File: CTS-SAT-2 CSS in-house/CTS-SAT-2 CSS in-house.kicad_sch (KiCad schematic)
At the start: 56 parts, among them J1 3v3, J2 GND, J3 SCL I2c, J4 SDA I2c, U1 POPA4383PWR, U2 POPA4383PWR, U3 ADS7128IRTET

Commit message: initial + footprints
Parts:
- LED1, LED2, LED3, LED4, LED5, LED6, LED7, LED8: footprint 6p550-5363p01-4_VIS -> 6p550-5363p01-4_VIS footprints:6p550-5363p01-4_VIS
- U1, U2: footprint TSSOP_PW_14_TEX -> ul_POPA4383PWR footprints:TSSOP_PW_14_TEX
- U3: footprint WQFN16_RTE_TEX -> WQFN16_RTE_TEX-M footprints:WQFN16_RTE_TEX
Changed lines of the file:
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@@
 			)
 		)
-		(property "Footprint" "6p550-5363p01-4_VIS"
+		(property "Footprint" "6p550-5363p01-4_VIS footprints:6p550-5363p01-4_VIS"
 			(at 180.34 25.4 0)
 			(hide yes)
@@
 			)
 		)
-		(property "Footprint" "6p550-5363p01-4_VIS"
+		(property "Footprint" "6p550-5363p01-4_VIS footprints:6p550-5363p01-4_VIS"
 			(at 58.42 78.74 0)
 			(hide yes)
@@
 			)
 		)
-		(property "Footprint" "WQFN16_RTE_TEX"
+		(property "Footprint" "WQFN16_RTE_TEX-M footprints:WQFN16_RTE_TEX"
 			(at 201.93 71.12 0)
 			(hide yes)
@@
 			)
 		)
-		(property "Footprint" "6p550-5363p01-4_VIS"
+		(property "Footprint" "6p550-5363p01-4_VIS footprints:6p550-5363p01-4_VIS"
 			(at 58.42 50.8 0)
 			(hide yes)
@@
 			)
 		)
-		(property "Footprint" "6p550-5363p01-4_VIS"
+		(property "Footprint" "6p550-5363p01-4_VIS footprints:6p550-5363p01-4_VIS"
 			(at 58.42 104.14 0)
 			(hide yes)
@@
 			)
 		)
-		(property "Footprint" "6p550-5363p01-4_VIS"
+		(property "Footprint" "6p550-5363p01-4_VIS footprints:6p550-5363p01-4_VIS"
 			(at 58.42 64.77 0)
 			(hide yes)
@@
 			)
 		)
-		(property "Footprint" "TSSOP_PW_14_TEX"
+		(property "Footprint" "ul_POPA4383PWR footprints:TSSOP_PW_14_TEX"
 			(at 97.79 27.94 0)
 			(hide yes)
@@
 			)
 		)
-		(property "Footprint" "6p550-5363p01-4_VIS"
+		(property "Footprint" "6p550-5363p01-4_VIS footprints:6p550-5363p01-4_VIS"
 			(at 58.42 36.83 0)
 			(hide yes)
@@
 			)
 		)
-		(property "Footprint" "6p550-5363p01-4_VIS"
+		(property "Footprint" "6p550-5363p01-4_VIS footprints:6p550-5363p01-4_VIS"
 			(at 58.42 20.32 0)
 			(hide yes)
@@
 			)
 		)
-		(property "Footprint" "6p550-5363p01-4_VIS"
+		(property "Footprint" "6p550-5363p01-4_VIS footprints:6p550-5363p01-4_VIS"
 			(at 58.42 91.44 0)
 			(hide yes)
@@
 			)
 		)
-		(property "Footprint" "TSSOP_PW_14_TEX"
+		(property "Footprint" "ul_POPA4383PWR footprints:TSSOP_PW_14_TEX"
 			(at 99.06 85.09 0)
 			(hide yes)

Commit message: Reorganized Schematic
Reorganized the structure of the schematic, using boxes and labels. Eliminated anything that was overlapping and improved readability.
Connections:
- net at C14.2, C4.2, R15.2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: no longer U3.16 (AIN1/GPIO1)
- net ARRAY_SIGNAL_4: now reaches C15.1, C6.1, LED5.1 (ANODE), R16.1, U2.2 (-IN_A)
- net TIA_OUTPUT_4: now reaches C15.2, C6.2, R6.2, U2.1 (OUT_A), U3.3 (AIN4/GPIO4)
- net ARRAY_SIGNAL_6: now reaches C11.1, C17.1, R8.1, U2.13 (-IN_D)
- net ARRAY_SIGNAL_6: now also LED8.1 (ANODE); no longer LED7.1 (ANODE)
- net TIA_OUTPUT_6: now reaches C11.2, C17.2, R18.2, U2.14 (OUT_D)
- net TIA_OUTPUT_6: now also U3.5 (AIN6/GPIO6); no longer U3.4 (AIN5/GPIO5)
- net ARRAY_SIGNAL_7: now reaches C12.1, C18.1, R9.1, U2.9 (-IN_C)
- net ARRAY_SIGNAL_7: now also LED7.1 (ANODE); no longer LED8.1 (ANODE)
- net TIA_OUTPUT_7: now reaches C12.2, C18.2, R19.2, U2.8 (OUT_C)
- net TIA_OUTPUT_7: now also U3.6 (AIN7/GPIO7); no longer U3.5 (AIN6/GPIO6)
- net at C19.1, C20.1, J1.1 (Pin_1)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: no longer C21.2, C22.2
- net ARRAY_SIGNAL_5: now reaches C10.1, C16.1, LED6.1 (ANODE), R17.1, U2.6 (-IN_B)
- net TIA_OUTPUT_3: now reaches C13.2, C5.2, R14.2, U1.8 (OUT_C)
- net TIA_OUTPUT_3: now also U3.2 (AIN3/GPIO3); no longer U3.1 (AIN2/GPIO2)
- net TIA_OUPTUT_1: now reaches C2.2, C7.2, R12.2, U1.1 (OUT_A)
- net TIA_OUPTUT_1: now also U3.16 (AIN1/GPIO1); no longer U3.15 (AIN0/GPIO0)
- net TIA_OUTPUT_2: now reaches C3.2, C8.2, R13.2, U1.7 (OUT_B)
- net TIA_OUTPUT_2: now also U3.1 (AIN2/GPIO2); no longer U3.2 (AIN3/GPIO3)
- net TIA_OUTPUT_5: now reaches C10.2, C16.2, R7.2, U2.7 (OUT_B)
- net TIA_OUTPUT_5: now also U3.4 (AIN5/GPIO5); no longer U3.6 (AIN7/GPIO7)
- net ARRAY_SIGNAL_3: now reaches C13.1, C5.1, LED4.1 (ANODE), R5.1, U1.9 (-IN_C)
- net ARRAY_SIGNAL_2: now reaches C3.1, C8.1, LED3.1 (ANODE), R3.1, U1.6 (-IN_B)
- net ARRAY_SIGNAL_1: now reaches C2.1, C7.1, LED2.1 (ANODE), R2.1, U1.2 (-IN_A)
- net at R17.2: no longer R7.1
- net Earth renamed GND
- net GND: no longer U3.17 (GND)
- new net COARSE_TIA_OUTPUT: U3.15 (AIN0/GPIO0)
- now unconnected: J4.1 (Pin_1), R21.2, U3.14 (SDA)
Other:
- note added: "ADC"
- note added: "Photodiode Array"
- note added: "TIA 1 CIRCUIT"
- note added: "TIA 2 CIRCUIT"
- moved on the sheet: C10, C11, C12, C13, C14, C15, C16, C17, C18, C19, C2, C20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

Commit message: Fixing from comments
Changed some basic things from comments, organization, correcting footprints.
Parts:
- removed J1: 3v3, Connector_PinHeader_2.54mm:PinHeader_1x01_P2.54mm_Vertical, symbol Connector_Generic:Conn_01x01
- removed J2: GND, Connector_PinHeader_2.54mm:PinHeader_1x01_P2.54mm_Vertical, symbol Connector_Generic:Conn_01x01
- removed J3: SCL I2c, Connector_PinHeader_2.54mm:PinHeader_1x01_P2.54mm_Vertical, symbol Connector_Generic:Conn_01x01
- removed J4: SDA I2c, Connector_PinHeader_2.54mm:PinHeader_1x01_P2.54mm_Vertical, symbol Connector_Generic:Conn_01x01
- added J1: Conn_01x04_Socket, Connector:FanPinHeader_1x04_P2.54mm_Vertical, symbol Connector:Conn_01x04_Socket
- R10, R11: now not fitted
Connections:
- net GND: now also U3.17 (GND), J1.3 (Pin_3)
- net 3V3_POWER: now reaches C19.1, C20.1, R21.1, R22.1, U3.10 (DVDD), U3.7 (AVDD)
- net 3V3_POWER: now also J1.4 (Pin_4)
- net at R21.2: now also U3.14 (SDA), J1.1 (Pin_1)
- net at R22.2, U3.13 (SCL): now also J1.2 (Pin_2)
- net 3V3_SUPPLY_1: now reaches C22.2
- net 3V3_SUPPLY_2: now reaches C21.2

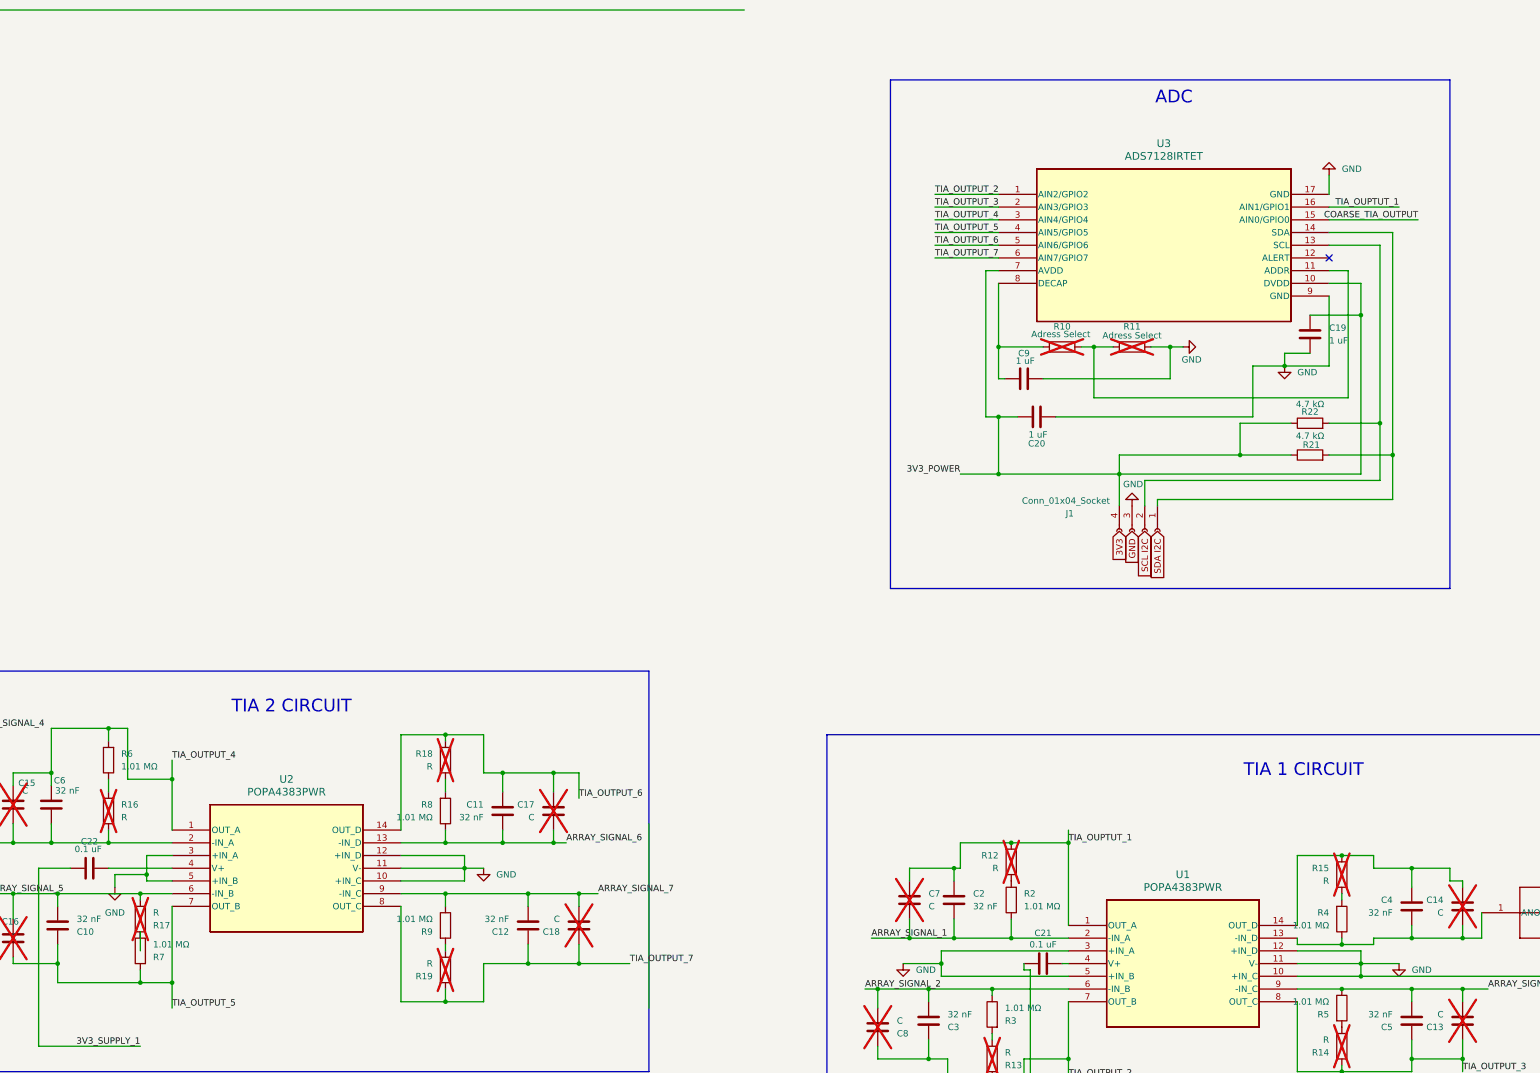
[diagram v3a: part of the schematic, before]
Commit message: More changes
Added voltage divider for virtual ground
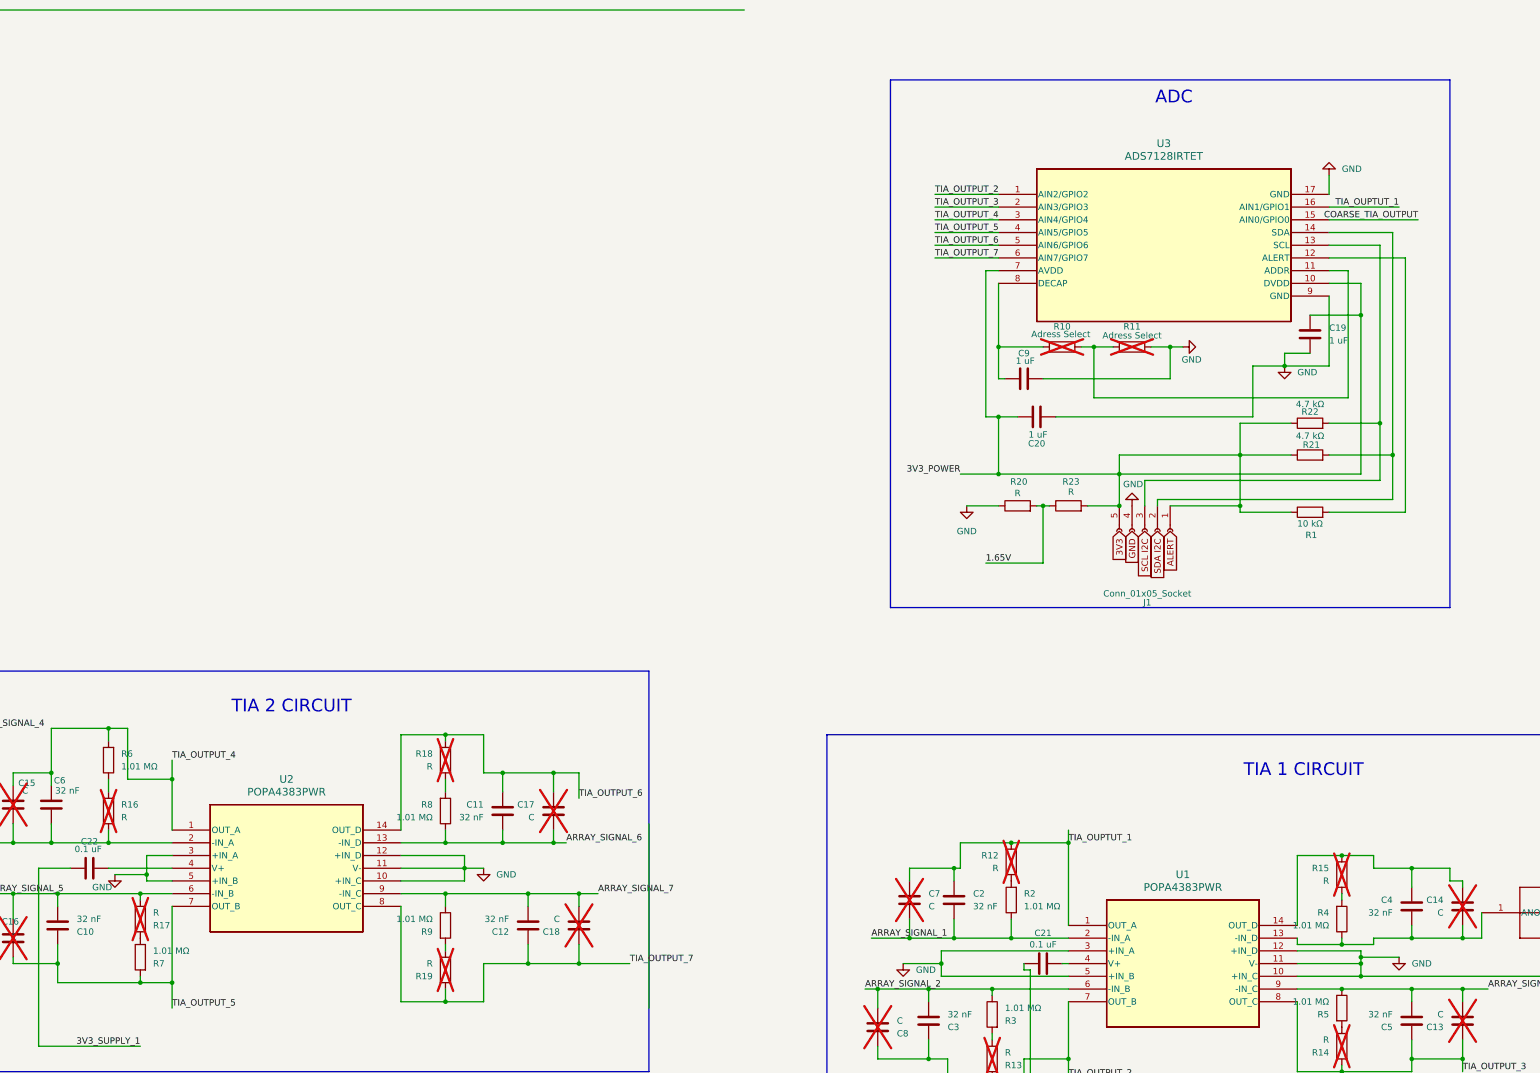
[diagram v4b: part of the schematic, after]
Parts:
- removed J1: Conn_01x04_Socket, Connector:FanPinHeader_1x04_P2.54mm_Vertical, symbol Connector:Conn_01x04_Socket
- added J1: Conn_01x05_Socket, symbol Connector:Conn_01x05_Socket
- added R1: 10 kΩ, Resistor_SMD:R_0201_0603Metric_Pad0.64x0.40mm_HandSolder, symbol Device:R
- added R20, R23: R, symbol Device:R
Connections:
- net 3V3_POWER: now also J1.1 (Pin_1), J1.5 (Pin_5), R1.1, R23.2
- net GND: now also J1.4 (Pin_4), R20.1
- net at R21.2, U3.14 (SDA): now also J1.2 (Pin_2)
- net at R22.2, U3.13 (SCL): now also J1.3 (Pin_3)
- net at U3.12 (ALERT): now also R1.2
- net at R17.2: now also R7.1
- new net 1.65V: R20.2, R23.1
- no-connect marks 1 -> 0
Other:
- moved on the sheet: R7

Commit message: Finished all comments
Completed all comments from the design review, changed DNP to sockets for testing, added virtual ground for TIAs, and other small things
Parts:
- removed C13, C14, C15, C16, C17, C18, C7, C8: C, Capacitor_SMD:C_1206_3216Metric_Pad1.33x1.80mm_HandSolder, symbol Device:C
- removed R12, R13, R14, R15, R16, R17, R18, R19: R, Resistor_SMD:R_1206_3216Metric_Pad1.30x1.75mm_HandSolder, symbol Device:R
- removed R21: 4.7 kΩ, Resistor_SMD:R_0603_1608Metric_Pad0.98x0.95mm_HandSolder, symbol Device:R
- added J10, J11, J12, J13, J14, J15, J16, J17, J2, J3, J4, J5, J6, J7, J8, J9: Socket_1x2, Connector_PinSocket_2.54mm:PinSocket_1x02_P2.54mm_Vertical, symbol Connector:Conn_01x02_Socket
- added R24: 4.7 kΩ, Resistor_SMD:R_0603_1608Metric_Pad0.98x0.95mm_HandSolder, symbol Device:R
- J1: footprint (none) -> Connector_PinHeader_2.54mm:PinHeader_1x05_P2.54mm_Vertical
- R20, R23: value R -> 10 kΩ; footprint (none) -> Resistor_SMD:R_0201_0603Metric_Pad0.64x0.40mm_HandSolder
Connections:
- net 3V3_SUPPLY_2 is gone; now on net 3V3_SUPPLY_1: C21.2
- net 3V3_SUPPLY_1: now also C19.1, C20.1, J1.5 (Pin_5), R1.1, R22.1, R23.2, U3.10 (DVDD), U3.7 (AVDD), R24.1
- net ARRAY_SIGNAL_1: now also J8.2 (Pin_2)
- net ARRAY_SIGNAL_2: now also J11.1 (Pin_1)
- net ARRAY_SIGNAL_3: now also J15.1 (Pin_1)
- net ARRAY_SIGNAL_4: now also J2.2 (Pin_2), J3.2 (Pin_2)
- net ARRAY_SIGNAL_5: now also J16.1 (Pin_1), J17.1 (Pin_1)
- net ARRAY_SIGNAL_6: now also J5.2 (Pin_2)
- net ARRAY_SIGNAL_7: now also J7.1 (Pin_1)
- net GND: no longer U1.10 (+IN_C), U1.12 (+IN_D), U1.3 (+IN_A), U1.5 (+IN_B), U2.10 (+IN_C), U2.12 (+IN_D), U2.3 (+IN_A), U2.5 (+IN_B)
- net TIA_OUPTUT_1: now also J8.1 (Pin_1), J9.1 (Pin_1)
- net TIA_OUTPUT_2: now also J10.2 (Pin_2), J11.2 (Pin_2)
- net TIA_OUTPUT_3: now also J14.2 (Pin_2), J15.2 (Pin_2)
- net TIA_OUTPUT_4: now also J2.1 (Pin_1)
- net TIA_OUTPUT_5: now also J16.2 (Pin_2)
- net TIA_OUTPUT_6: now also J4.1 (Pin_1), J5.1 (Pin_1)
- net TIA_OUTPUT_7: now also J6.2 (Pin_2), J7.2 (Pin_2)
- net at C4.1, LED1.1 (ANODE), R4.1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: now also J13.2 (Pin_2)
- net COURSE_TIA_OUTPUT: now reaches C4.2, U1.14 (OUT_D)
- net COURSE_TIA_OUTPUT: now also J12.1 (Pin_1), J13.1 (Pin_1)
- net at J1.2 (Pin_2): now also R22.2, U3.13 (SCL); no longer U3.14 (SDA)
- net at R1.2, U3.12 (ALERT): now also J1.3 (Pin_3)
- net at R3.2: now also J10.1 (Pin_1)
- net at R8.2: now also J4.2 (Pin_2)
- net at R4.2: now also J12.2 (Pin_2)
- net at R5.2: now also J14.1 (Pin_1)
- net at R9.2: now also J6.1 (Pin_1)
- net at R2.2: now also J9.2 (Pin_2)
- net at R7.1: now also J17.2 (Pin_2)
- net at R6.1: now also J3.1 (Pin_1)
- net 1.65V renamed 1.65V_VGND_1
- net 1.65V_VGND_1: now also U1.10 (+IN_C), U1.12 (+IN_D), U1.3 (+IN_A), U1.5 (+IN_B), U2.3 (+IN_A), U2.5 (+IN_B)
- removed net 3V3_POWER: C19.1, C20.1, J1.1 (Pin_1), J1.5 (Pin_5), R1.1, R22.1, R23.2, U3.10 (DVDD), U3.7 (AVDD)
- new net: J1.1 (Pin_1), R24.2, U3.14 (SDA)
- new net 1.65V_VGND: U2.10 (+IN_C), U2.12 (+IN_D)
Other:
- note added: "MCU pins"
- note added: "Pull-Up Resistors for I2C and ALERT"
- note added: "Voltage Splitter"
- moved on the sheet: C19, C20, C9, R1, R10, R11, R20, R22, R23, U3

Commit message: More work on PCB routing
Rough draft
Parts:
- removed R10, R11: Adress Select, Resistor_SMD:R_1206_3216Metric_Pad1.30x1.75mm_HandSolder, symbol Device:R
- added J18, J19: Socket_1x2, Connector_PinSocket_2.54mm:PinSocket_1x02_P2.54mm_Vertical_SMD_Pin1Left, symbol Connector:Conn_01x02_Socket
- J10, J11, J12, J13, J14, J15, J16, J17, J2, J3, J4, J5, J6, J7, J8, J9: footprint Connector_PinSocket_2.54mm:PinSocket_1x02_P2.54mm_Vertical -> Connector_PinSocket_2.54mm:PinSocket_1x02_P2.54mm_Vertical_SMD_Pin1Left
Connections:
- net 1.65V_VGND is gone; now on net 1.65V_VGND_1: U2.10 (+IN_C), U2.12 (+IN_D)
- net GND: now also J19.1 (Pin_1)
- net at C9.2, U3.8 (DECAP): now also J18.2 (Pin_2)
- net at U3.11 (ADDR): now also J18.1 (Pin_1), J19.2 (Pin_2)

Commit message: Minor changes
Minor revisions
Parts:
- removed J10, J11, J14, J15, J16, J17, J2, J3, J4, J5, J6, J7, J8, J9: Socket_1x2, Connector_PinSocket_2.54mm:PinSocket_1x02_P2.54mm_Vertical_SMD_Pin1Left, symbol Connector:Conn_01x02_Socket
- added C1, C13, C14, C15, C16, C7, C8: C, Capacitor_SMD:C_0603_1608Metric_Pad1.08x0.95mm_HandSolder, symbol Device:C
- added R10, R11, R12, R13, R14, R15, R16: R, Resistor_SMD:R_0603_1608Metric_Pad0.98x0.95mm_HandSolder, symbol Device:R
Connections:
- net ARRAY_SIGNAL_1: now also C15.2
- net ARRAY_SIGNAL_2: now also C14.1
- net ARRAY_SIGNAL_3: now also C16.1
- net ARRAY_SIGNAL_4: now also C7.2, R11.2
- net ARRAY_SIGNAL_5: now also C1.1, R10.1
- net ARRAY_SIGNAL_6: now also C8.2
- net ARRAY_SIGNAL_7: now also C13.1
- net TIA_OUPTUT_1: now also C15.1, R15.1
- net TIA_OUTPUT_2: now also C14.2, R14.2
- net TIA_OUTPUT_3: now also C16.2, R16.2
- net TIA_OUTPUT_4: now also C7.1
- net TIA_OUTPUT_5: now also C1.2
- net TIA_OUTPUT_6: now also C8.1, R12.1
- net TIA_OUTPUT_7: now also C13.2, R13.2
- net at R3.2: now also R14.1
- net at R7.1: now also R10.2
- net at R9.2: now also R13.1
- net at R5.2: now also R16.1
- net at R8.2: now also R12.2
- net at R6.1: now also R11.1
- net at R2.2: now also R15.2
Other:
- moved on the sheet: R2, R7

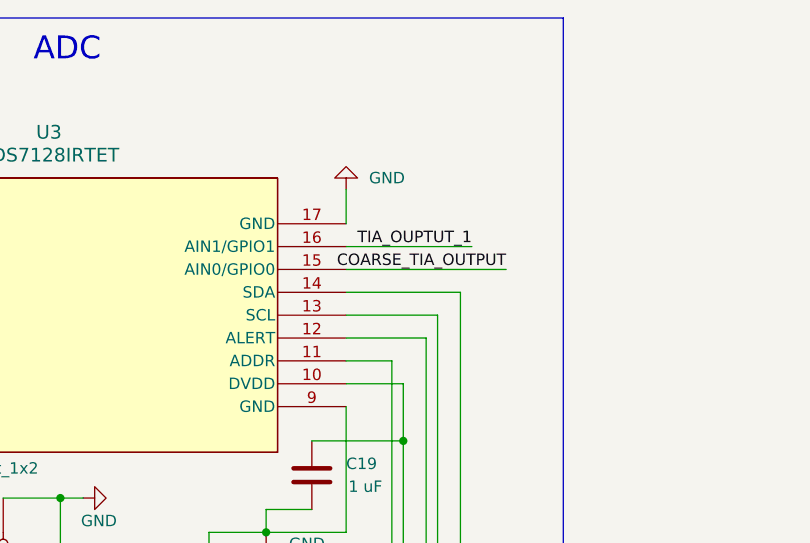
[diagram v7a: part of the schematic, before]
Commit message: PCB routing first draft
Generally routed the pcb, still drc errors and other things need fixing
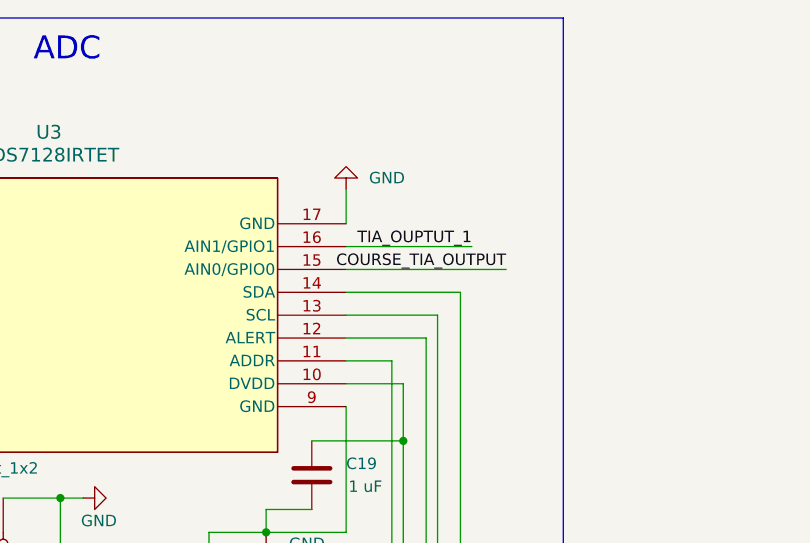
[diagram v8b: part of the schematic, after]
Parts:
- R1: footprint Resistor_SMD:R_0201_0603Metric_Pad0.64x0.40mm_HandSolder -> Resistor_SMD:R_0603_1608Metric_Pad0.98x0.95mm_HandSolder
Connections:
- net COARSE_TIA_OUTPUT is gone; now on net COURSE_TIA_OUTPUT: U3.15 (AIN0/GPIO0)
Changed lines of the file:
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@@
 		)
 	)
-	(label "COARSE_TIA_OUTPUT"
+	(label "COURSE_TIA_OUTPUT"
 		(at 412.75 41.91 180)
 		(effects
@@
 			)
 		)
-		(property "Footprint" "Resistor_SMD:R_0201_0603Metric_Pad0.64x0.40mm_HandSolder"
+		(property "Footprint" "Resistor_SMD:R_0603_1608Metric_Pad0.98x0.95mm_HandSolder"
 			(at 391.16 86.868 90)
 			(hide yes)
